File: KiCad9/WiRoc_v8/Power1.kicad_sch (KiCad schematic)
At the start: 11 parts, among them Q1 L2N7002WT1G, U18 MP2143DJ

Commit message: etc
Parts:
- C94: LCSC Part # (none) -> C1555; Manufacturer (none) -> Murata Electronics; ManufacturerPartNumber (none) -> GRM155R71C223JA01D
- R55: LCSC Part # (none) -> C25804; Manufacturer (none) -> Uniroyal Elec; ManufacturerPartNumber (none) -> 0603WAF1002T5E
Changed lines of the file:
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@@
+			)
+		)
+		(property "LCSC Part #" "C25804"
+			(at 191.77 127 0)
+			(effects
+				(font
+					(size 1.27 1.27)
+				)
+				(hide yes)
+			)
+		)
+		(property "Manufacturer" "Uniroyal Elec"
+			(at 191.77 127 0)
+			(effects
+				(font
+					(size 1.27 1.27)
+				)
+				(hide yes)
+			)
+		)
+		(property "ManufacturerPartNumber" "0603WAF1002T5E"
+			(at 191.77 127 0)
+			(effects
+				(font
+					(size 1.27 1.27)
+				)
+				(hide yes)
 			)
 		)
@@
 			(at 162.56 104.14 0)
 			(effects
+				(font
+					(size 1.27 1.27)
+				)
+				(hide yes)
+			)
+		)
+		(property "LCSC Part #" "C1555"
+			(at 162.56 104.14 0)
+			(effects
+				(font
+					(size 1.27 1.27)
+				)
+				(hide yes)
+			)
+		)
+		(property "Manufacturer" "Murata Electronics"
+			(at 162.56 104.14 0)
+			(effects
+				(font
+					(size 1.27 1.27)
+				)
+				(hide yes)
+			)
+		)
+		(property "ManufacturerPartNumber" "GRM155R71C223JA01D"
+			(at 162.56 104.14 0)
+			(effects

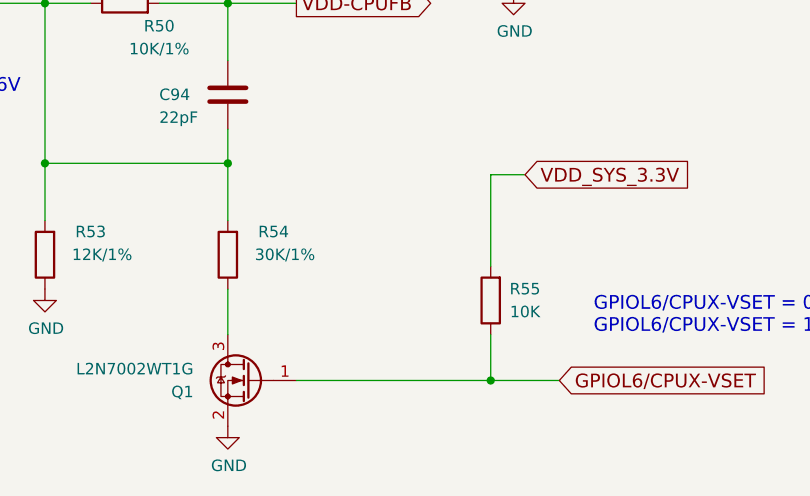
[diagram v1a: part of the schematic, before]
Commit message: add bom
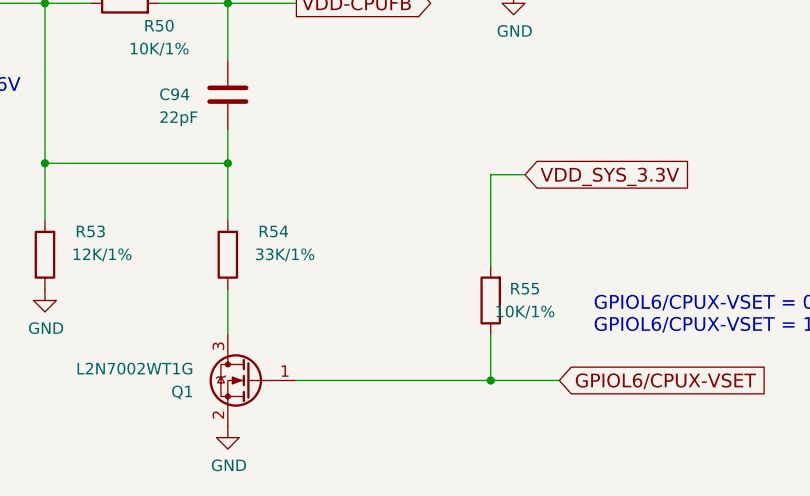
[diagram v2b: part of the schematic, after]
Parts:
- C93, C95, C96: IncludeInBOM (none) -> TRUE; JLCBasicExtended (none) -> Basic; LCSC Part # (none) -> C15525; Manufacturer (none) -> Samsung Electro-Mechanics; ManufacturerPartNumber (none) -> CL05A106MQ5NUNC; Package (none) -> 0402
- C94: IncludeInBOM (none) -> TRUE; JLCBasicExtended (none) -> Basic; Package (none) -> 0402
- L6: IncludeInBOM (none) -> TRUE; JLCBasicExtended (none) -> Extended; LCSC Part # (none) -> C521238; Manufacturer (none) -> Murata Electronics; ManufacturerPartNumber (none) -> DFE252010P-1R0M=P2; Package (none) -> 1008
- Q1: IncludeInBOM (none) -> TRUE; JLCBasicExtended (none) -> Extended; LCSC Part # (none) -> C12778; Manufacturer (none) -> LRC; ManufacturerPartNumber (none) -> L2N7002WT1G; Package (none) -> SOT-323
- R50: IncludeInBOM (none) -> TRUE; JLCBasicExtended (none) -> Basic; LCSC Part # (none) -> C25744; Manufacturer (none) -> Uniroyal Elec; ManufacturerPartNumber (none) -> 0402WGF1002TCE; Package (none) -> 0402
- R53: IncludeInBOM (none) -> TRUE; JLCBasicExtended (none) -> Basic; LCSC Part # (none) -> C25752; Manufacturer (none) -> Uniroyal Elec; ManufacturerPartNumber (none) -> 0402WGF1202TCE; Package (none) -> 0402
- R54: value 30K/1% -> 33K/1%; IncludeInBOM (none) -> TRUE; JLCBasicExtended (none) -> Basic; LCSC Part # (none) -> C25779; Manufacturer (none) -> Uniroyal Elec; ManufacturerPartNumber (none) -> 0402WGF3302TCE; Note (none) -> 30K ohm ideal for 1.3, but 33Kohm should be close enough; Package (none) -> 0402
- R55: value 10K -> 10K/1%; IncludeInBOM (none) -> TRUE; JLCBasicExtended (none) -> Basic; LCSC Part # C25804 -> C25744; ManufacturerPartNumber 0603WAF1002T5E -> 0402WGF1002TCE; Package (none) -> 0402
- U18: IncludeInBOM (none) -> TRUE; JLCBasicExtended (none) -> Extended; LCSC Part # (none) -> C43427; Manufacturer (none) -> Monolithic Power Systems; ManufacturerPartNumber (none) -> MP2143DJ-LF-Z; Package (none) -> TSOT-23-8

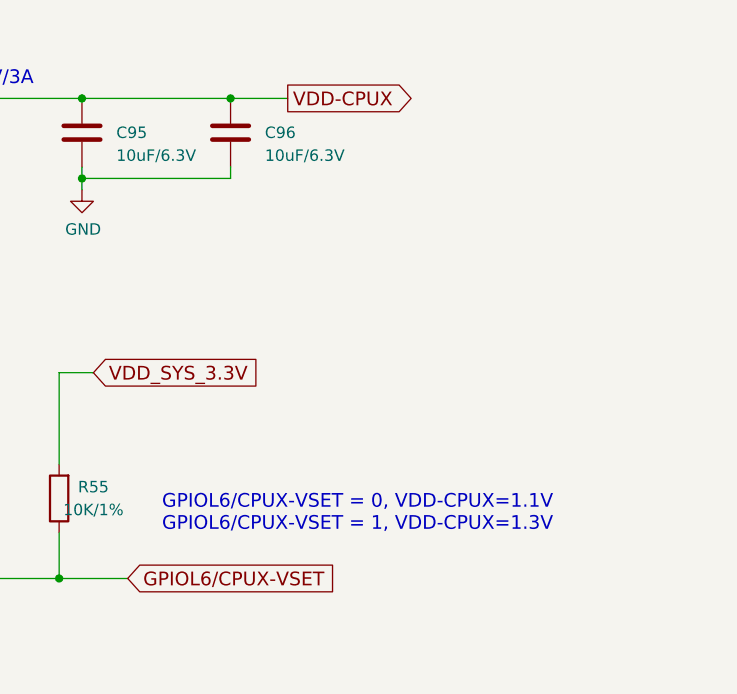
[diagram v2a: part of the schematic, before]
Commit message: add esp32hosted-c5 board
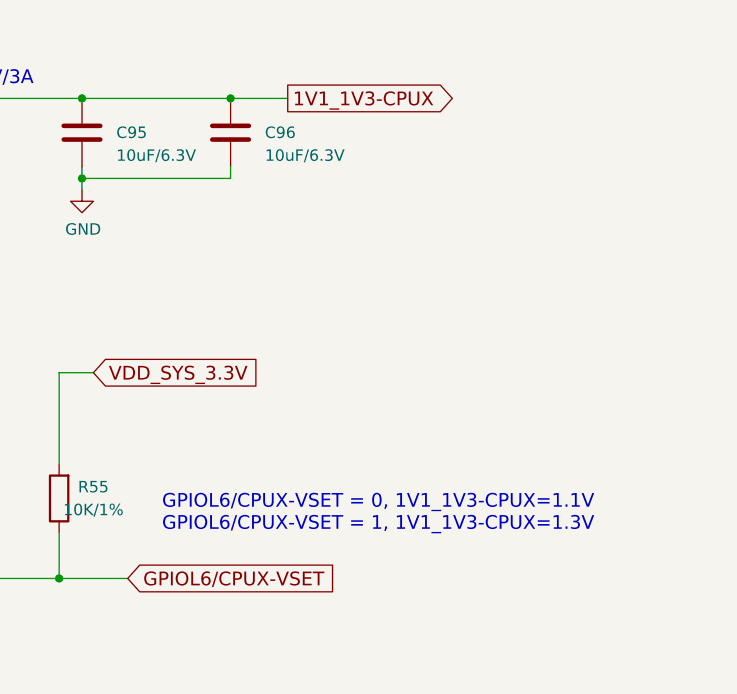
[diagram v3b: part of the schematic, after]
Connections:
- net VDD-CPUX renamed 1V1_1V3-CPUX
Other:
- note added: "GPIOL6/CPUX-VSET = 0, 1V1_1V3-CPUX=1.1V GPIOL6/CPUX-VSET = 1, 1V1_1V3-CPUX=1.3V"
- note removed: "GPIOL6/CPUX-VSET = 0, VDD-CPUX=1.1V GPIOL6/CPUX-VSET = 1, VDD-CPUX=1.3V"
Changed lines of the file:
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@@
 	(generator_version "9.0")
 	(paper "A4")
-	(text "GPIOL6/CPUX-VSET = 0, VDD-CPUX=1.1V\nGPIOL6/CPUX-VSET = 1, VDD-CPUX=1.3V"
+	(text "GPIOL6/CPUX-VSET = 0, 1V1_1V3-CPUX=1.1V\nGPIOL6/CPUX-VSET = 1, 1V1_1V3-CPUX=1.3V"
 		(exclude_from_sim no)
 		(at 203.2 130.81 0)
@@
 		)
 	)
-	(global_label "VDD-CPUX"
+	(global_label "1V1_1V3-CPUX"
 		(shape output)
 		(at 217.17 82.55 0)
@@
 		)
 		(property "Intersheetrefs" "${INTERSHEET_REFS}"
-			(at 232.304 82.55 0)
+			(at 237.529 82.55 0)
 			(effects
 				(font

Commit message: save point for fix to layer issues in6
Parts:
- C93, C95, C96: value 10uF/6.3V -> 10uF

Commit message: many small changes, change eMMC
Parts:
- C93, C95, C96: value 10uF -> 10uF/6.3V
- C94: Manufacturer Murata Electronics -> FH (Guangdong Fenghua Advanced Tech); ManufacturerPartNumber GRM155R71C223JA01D -> 0402CG220J500NT
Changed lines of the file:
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@@
 			)
 		)
-		(property "Value" "10uF"
+		(property "Value" "10uF/6.3V"
 			(at 198.12 88.9 0)
 			(effects
@@
 			)
 		)
-		(property "Value" "10uF"
+		(property "Value" "10uF/6.3V"
 			(at 214.63 88.9 0)
 			(effects
@@
 			)
 		)
-		(property "Value" "10uF"
+		(property "Value" "10uF/6.3V"
 			(at 77.47 92.71 0)
 			(effects
@@
 			)
 		)
-		(property "Manufacturer" "Murata Electronics"
+		(property "Manufacturer" "FH (Guangdong Fenghua Advanced Tech)"
 			(at 162.56 104.14 0)
 			(effects
@@
 			)
 		)
-		(property "ManufacturerPartNumber" "GRM155R71C223JA01D"
+		(property "ManufacturerPartNumber" "0402CG220J500NT"
 			(at 162.56 104.14 0)
 			(effects

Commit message: etc
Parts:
- Q1: FT Rotation Offset (none) -> 180
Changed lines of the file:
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@@
+			)
+		)
+		(property "FT Rotation Offset" "180"
+			(at 165.1 135.89 0)
+			(effects
+				(font
+					(size 1.27 1.27)
+				)
+				(hide yes)
 			)
 		)
